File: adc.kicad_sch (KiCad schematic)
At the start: 7 parts, among them U6 LTC2299xUP

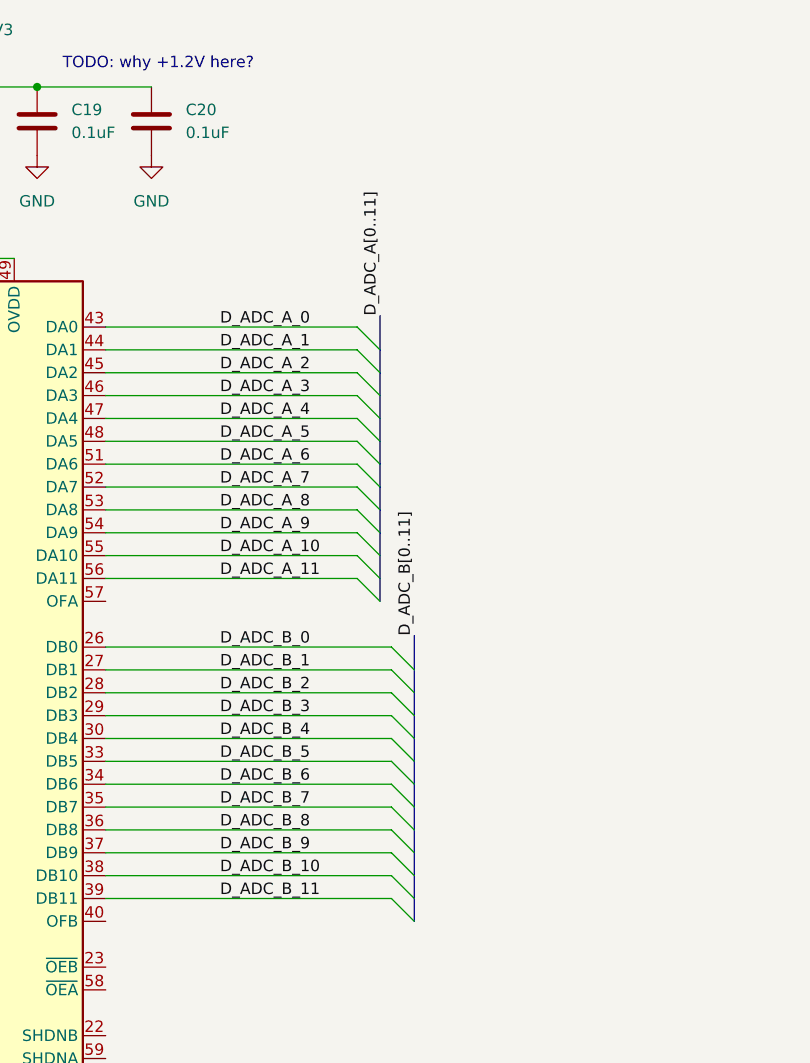
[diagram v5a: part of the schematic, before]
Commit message: Link up ADC to FPGA
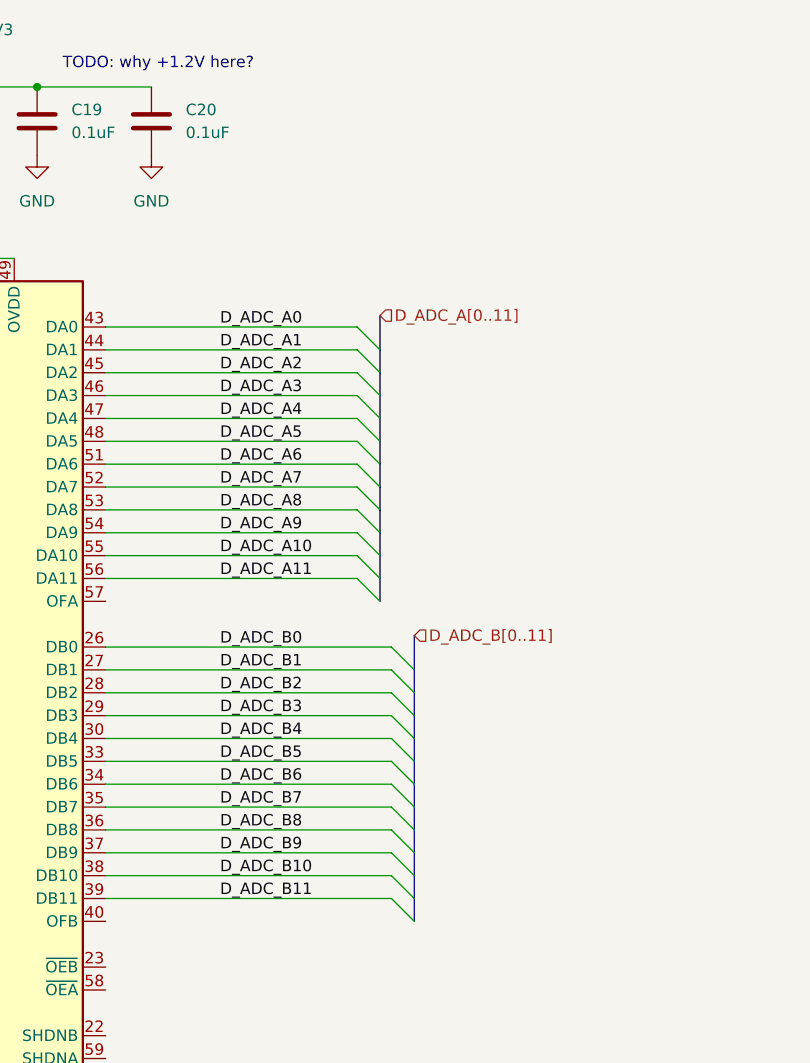
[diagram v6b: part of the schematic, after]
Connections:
- net D_ADC_A_0 renamed D_ADC_A0
- net D_ADC_A_1 renamed D_ADC_A1
- net D_ADC_A_10 renamed D_ADC_A10
- net D_ADC_A_11 renamed D_ADC_A11
- net D_ADC_A_2 renamed D_ADC_A2
- net D_ADC_A_3 renamed D_ADC_A3
- net D_ADC_A_4 renamed D_ADC_A4
- net D_ADC_A_5 renamed D_ADC_A5
- net D_ADC_A_6 renamed D_ADC_A6
- net D_ADC_A_7 renamed D_ADC_A7
- net D_ADC_A_8 renamed D_ADC_A8
- net D_ADC_A_9 renamed D_ADC_A9
- net D_ADC_B_0 renamed D_ADC_B0
- net D_ADC_B_1 renamed D_ADC_B1
- net D_ADC_B_10 renamed D_ADC_B10
- net D_ADC_B_11 renamed D_ADC_B11
- net D_ADC_B_2 renamed D_ADC_B2
- net D_ADC_B_3 renamed D_ADC_B3
- net D_ADC_B_4 renamed D_ADC_B4
- net D_ADC_B_5 renamed D_ADC_B5
- net D_ADC_B_6 renamed D_ADC_B6
- net D_ADC_B_7 renamed D_ADC_B7
- net D_ADC_B_8 renamed D_ADC_B8
- net D_ADC_B_9 renamed D_ADC_B9
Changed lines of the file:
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@@
 		)
 	)
-	(label "D_ADC_A_5"
+	(label "D_ADC_B9"
+		(at 171.45 114.3 0)
+		(effects
+			(font
+				(size 1.27 1.27)
+			)
+			(justify left bottom)
+		)
+	)
+	(label "D_ADC_B3"
+		(at 171.45 99.06 0)
+		(effects
+			(font
+				(size 1.27 1.27)
+			)
+			(justify left bottom)
+		)
+	)
+	(label "D_ADC_A11"
+		(at 171.45 83.82 0)
+		(effects
+			(font
+				(size 1.27 1.27)
+			)
+			(justify left bottom)
+		)
+	)
+	(label "D_ADC_B7"
+		(at 171.45 109.22 0)
+		(effects
+			(font
+				(size 1.27 1.27)
+			)
+			(justify left bottom)
+		)
+	)
+	(label "D_ADC_A8"
+		(at 171.45 76.2 0)
+		(effects
+			(font
+				(size 1.27 1.27)
+			)
+			(justify left bottom)
+		)
+	)
+	(label "D_ADC_A10"
+		(at 171.45 81.28 0)
+		(effects
+			(font
+				(size 1.27 1.27)
+			)
+			(justify left bottom)
+		)
+	)
+	(label "D_ADC_A5"
 		(at 171.45 68.58 0)
 		(effects
@@
 		)
 	)
-	(label "D_ADC_B_4"
+	(label "D_ADC_B0"
+		(at 171.45 91.44 0)
+		(effects
+			(font
+				(size 1.27 1.27)
+			)
+			(justify left bottom)
+		)
+	)
+	(label "D_ADC_B6"
+		(at 171.45 106.68 0)
+		(effects
+			(font
+				(size 1.27 1.27)
+			)
+			(justify left bottom)
+		)
+	)
+	(label "D_ADC_A7"
+		(at 171.45 73.66 0)
+		(effects
+			(font
+				(size 1.27 1.27)
+			)
+			(justify left bottom)
+		)
+	)
+	(label "D_ADC_A0"
+		(at 171.45 55.88 0)
+		(effects
+			(font
+				(size 1.27 1.27)
+			)
+			(justify left bottom)
+		)
+	)
+	(label "D_ADC_A3"
+		(at 171.45 63.5 0)
+		(effects
+			(font
+				(size 1.27 1.27)
+			)
+			(justify left bottom)
+		)
+	)
+	(label "D_ADC_B2"
+		(at 171.45 96.52 0)
+		(effects
+			(font
+				(size 1.27 1.27)
+			)
+			(justify left bottom)
+		)
+	)
+	(label "D_ADC_A4"
+		(at 171.45 66.04 0)
+		(effects
+			(font
+				(size 1.27 1.27)
+			)
+			(justify left bottom)
+		)
+	)
+	(label "D_ADC_A2"
+		(at 171.45 60.96 0)
+		(effects
+			(font
+				(size 1.27 1.27)
+			)
+			(justify left bottom)
+		)
+	)
+	(label "D_ADC_A6"
+		(at 171.45 71.12 0)
+		(effects
+			(font
+				(size 1.27 1.27)
+			)
+			(justify left bottom)
+		)
+	)
+	(label "D_ADC_B4"
 		(at 171.45 101.6 0)
 		(effects
@@
 		)
 	)
-	(label "D_ADC_A_9"
+	(label "D_ADC_B10"
+		(at 171.45 116.84 0)
+		(effects
+			(font
+				(size 1.27 1.27)
+			)
+			(justify left bottom)
+		)
+	)
+	(label "D_ADC_B8"
+		(at 171.45 111.76 0)
+		(effects
+			(font
+				(size 1.27 1.27)
+			)
+			(justify left bottom)
+		)
+	)
+	(label "D_ADC_B1"
+		(at 171.45 93.98 0)
+		(effects
+			(font
+				(size 1.27 1.27)
+			)
+			(justify left bottom)
+		)
+	)
+	(label "D_ADC_B11"
+		(at 171.45 119.38 0)
+		(effects
+			(font
+				(size 1.27 1.27)
+			)
+			(justify left bottom)
+		)
+	)
+	(label "D_ADC_B5"
+		(at 171.45 104.14 0)
+		(effects
+			(font
+				(size 1.27 1.27)
+			)
+			(justify left bottom)
+		)
+	)
+	(label "D_ADC_A1"
+		(at 171.45 58.42 0)
+		(effects
+			(font
+				(size 1.27 1.27)
+			)
+			(justify left bottom)
+		)
+	)
+	(label "D_ADC_A9"
 		(at 171.45 78.74 0)
 		(effects
@@
 		)
 	)
-	(label "D_ADC_A_6"
-		(at 171.45 71.12 0)
-		(effects
-			(font
-				(size 1.27 1.27)
-			)
-			(justify left bottom)
-		)
-	)
-	(label "D_ADC_B_7"
-		(at 171.45 109.22 0)
-		(effects
-			(font
-				(size 1.27 1.27)
-			)
-			(justify left bottom)
-		)
-	)
-	(label "D_ADC_B_8"
-		(at 171.45 111.76 0)
-		(effects
-			(font
-				(size 1.27 1.27)
-			)
-			(justify left bottom)
-		)
-	)
-	(label "D_ADC_A_10"
-		(at 171.45 81.28 0)
-		(effects
-			(font
-				(size 1.27 1.27)
-			)
-			(justify left bottom)
-		)
-	)
-	(label "D_ADC_A_3"
-		(at 171.45 63.5 0)
-		(effects
-			(font
-				(size 1.27 1.27)
-			)
-			(justify left bottom)
-		)
-	)
-	(label "D_ADC_A_1"
-		(at 171.45 58.42 0)
-		(effects
-			(font
-				(size 1.27 1.27)
-			)
-			(justify left bottom)
-		)
-	)
-	(label "D_ADC_B_2"
-		(at 171.45 96.52 0)
-		(effects
-			(font
-				(size 1.27 1.27)
-			)
-			(justify left bottom)
-		)
-	)
-	(label "D_ADC_A_8"
-		(at 171.45 76.2 0)
-		(effects
-			(font
-				(size 1.27 1.27)
-			)
-			(justify left bottom)
-		)
-	)
-	(label "D_ADC_B_5"
-		(at 171.45 104.14 0)
-		(effects
-			(font
-				(size 1.27 1.27)
-			)
-			(justify left bottom)
-		)
-	)
-	(label "D_ADC_A_11"
-		(at 171.45 83.82 0)
-		(effects
-			(font
-				(size 1.27 1.27)
-			)
-			(justify left bottom)
-		)
-	)
-	(label "D_ADC_A_4"
-		(at 171.45 66.04 0)
-		(effects
-			(font
-				(size 1.27 1.27)
-			)
-			(justify left bottom)
-		)
-	)
-	(label "D_ADC_B_1"
-		(at 171.45 93.98 0)
-		(effects
-			(font
-				(size 1.27 1.27)
-			)
-			(justify left bottom)
-		)
-	)
-	(label "D_ADC_B_9"
-		(at 171.45 114.3 0)
-		(effects
-			(font
-				(size 1.27 1.27)
-			)
-			(justify left bottom)
-		)
-	)
-	(label "D_ADC_A_2"
-		(at 171.45 60.96 0)
-		(effects
-			(font
-				(size 1.27 1.27)
-			)
-			(justify left bottom)
-		)
-	)
-	(label "D_ADC_A_0"
-		(at 171.45 55.88 0)
-		(effects
-			(font
-				(size 1.27 1.27)
-			)
-			(justify left bottom)
-		)
-	)
-	(label "D_ADC_B_0"
-		(at 171.45 91.44 0)
-		(effects
-			(font
-				(size 1.27 1.27)
-			)
-			(justify left bottom)
-		)
-	)
-	(label "D_ADC_A_7"
-		(at 171.45 73.66 0)
-		(effects
-			(font
-				(size 1.27 1.27)
-			)
-			(justify left bottom)
-		)
-	)
-	(label "D_ADC_B[0..11]"
-		(at 193.04 90.17 90)
-		(effects
-			(font
-				(size 1.27 1.27)
-			)
-			(justify left bottom)
-		)
-	)
-	(label "D_ADC_B_10"
-		(at 171.45 116.84 0)
-		(effects
-			(font
-				(size 1.27 1.27)
-			)
-			(justify left bottom)
-		)
-	)
-	(label "D_ADC_B_3"
-		(at 171.45 99.06 0)
-		(effects
-			(font
-				(size 1.27 1.27)
-			)
-			(justify left bottom)
-		)
-	)
-	(label "D_ADC_A[0..11]"
-		(at 189.23 54.61 90)
-		(effects
-			(font
-				(size 1.27 1.27)
-			)
-			(justify left bottom)
-		)
-	)
-	(label "D_ADC_B_11"
-		(at 171.45 119.38 0)
-		(effects
-			(font
-				(size 1.27 1.27)
-			)
-			(justify left bottom)
-		)
-	)
-	(label "D_ADC_B_6"
-		(at 171.45 106.68 0)
-		(effects
-			(font
-				(size 1.27 1.27)
-			)
-			(justify left bottom)
-		)
-	)
 	(global_label "CH2_CH-"
 		(shape input)
@@
 		)
 	)
+	(hierarchical_label "D_ADC_B[0..11]"
+		(shape input)
+		(at 193.04 90.17 0)
+		(effects
+			(font
+				(size 1.27 1.27)
+			)
+			(justify left)
+		)
+	)
+	(hierarchical_label "D_ADC_A[0..11]"
+		(shape input)
+		(at 189.23 54.61 0)
+		(effects
+			(font
+				(size 1.27 1.27)
+			)
+			(justify left)
+		)
+	)

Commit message: Save work on simplifying the desing
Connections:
- net CH2_COMMON is gone; now on net +1V5: C15.1, U6.20 (VCMB)
- net CH1_COMMON renamed +1V5
